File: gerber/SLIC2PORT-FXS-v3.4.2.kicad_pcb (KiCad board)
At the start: 2 copper layers, 120 x 90 mm, 160 parts, among them J1 USB-C_PWR, J2 DC5V_IN, J5 EXPANSION, J6 UART_DBG, K1 G5V-2_DC5, K2 G5V-2_DC5, Q1 AO3401A, Q2 2N7002, Q3 2N7002, Q4 2N7002, Q5 2N7002, Q6 2N7002, SW1 RST, SW2 BOOT, U1 M5StampS3/S3A, U106 1N5819, U2 74HCT244, U45 1N4007, U49 1N4007, U55 P3100SC, U56 1N4007, U57 1N4007, U58 1N4007, U59 1N4007, U60 BZT03C82, U64 BK2125HS601-T, U79 1N5819, U82 P3100SC, U83 1N4007, U84 1N4007, U85 1N4007, U86 1N4007, U87 BZT03C82, U91 BK2125HS601-T

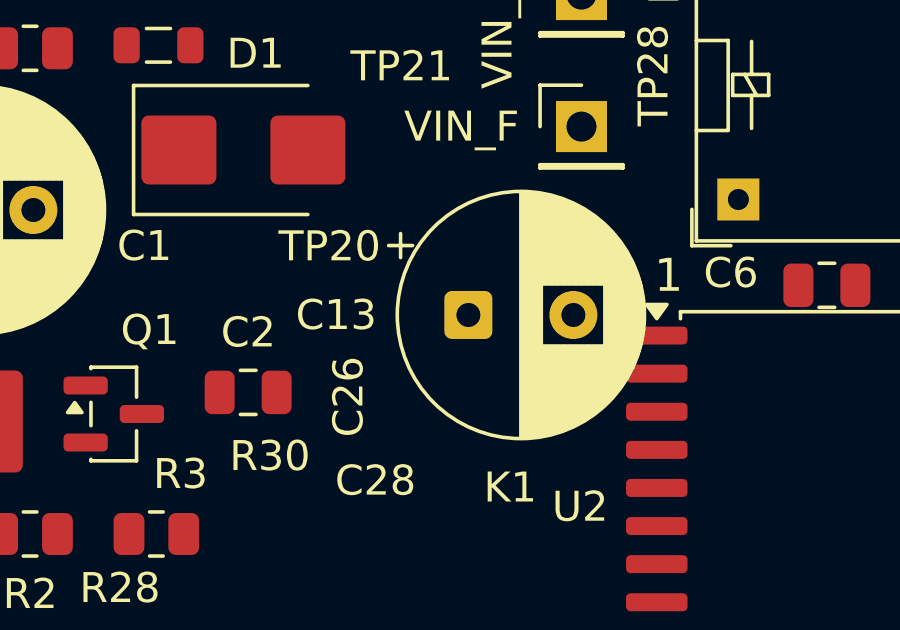
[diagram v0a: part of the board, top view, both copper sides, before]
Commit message: board v3.4.2: 第9ラウンド処方 (C13 -1.0mm) を適用し第10ラウンドとして記録
- C13 を X -1.00mm へ移動 (生成元にも同期、check_regen 0/0 維持)。
  U2 パッド1/2 との干渉 -0.474/-0.124mm -> +0.521/+0.799mm を実測で再現
- RJ11 是正ラウンドは監査側の第9ラウンド (コンデンサ監査) と重なるため
  第10ラウンドとして CAD_REPORT に記録し、生成元の表記も round 10 に整合
- README_CAD の RJ11 項を想定寸法から指定部品の実寸仕様へ更新
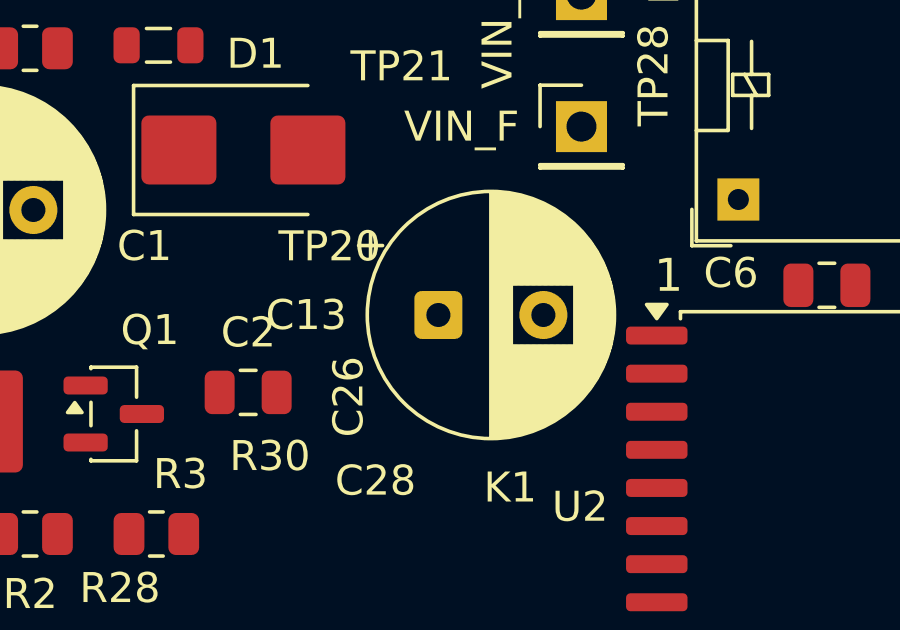
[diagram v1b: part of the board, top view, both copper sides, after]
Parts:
- moved C13 1.00 mm to (21.5, 65.3)
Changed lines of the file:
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@@
 		)
 		(attr through_hole)
+		(duplicate_pad_numbers_are_jumpers no)
 		(fp_line
-			(start -6.10 -6.00)
-			(end 6.10 -6.00)
+			(start -6.1 -6)
+			(end 6.1 -6)
 			(stroke
 				(width 0.12)
@@
 		)
 		(fp_line
-			(start 6.10 -6.00)
-			(end 6.10 9.00)
+			(start -6.1 9)
+			(end -6.1 -6)
 			(stroke
 				(width 0.12)
@@
 		)
 		(fp_line
-			(start 6.10 9.00)
-			(end -6.10 9.00)
+			(start 6.1 -6)
+			(end 6.1 9)
 			(stroke
 				(width 0.12)
@@
 		)
 		(fp_line
-			(start -6.10 9.00)
-			(end -6.10 -6.00)
+			(start 6.1 9)
+			(end -6.1 9)
 			(stroke
 				(width 0.12)
@@
 			(layer "F.SilkS")
 		)
-		(fp_line
-			(start -6.35 -6.30)
-			(end 6.35 -6.30)
+		(fp_circle
+			(center 4.35 4.64)
+			(end 4.85 4.64)
 			(stroke
-				(width 0.05)
+				(width 0.12)
 				(type solid)
 			)
-			(layer "F.CrtYd")
+			(fill no)
+			(layer "F.SilkS")
 		)
 		(fp_line
-			(start 6.35 -6.30)
-			(end 6.35 9.30)
+			(start -6.35 -6.3)
+			(end 6.35 -6.3)
 			(stroke
 				(width 0.05)
@@
 		)
 		(fp_line
-			(start 6.35 9.30)
-			(end -6.35 9.30)
+			(start -6.35 9.3)
+			(end -6.35 -6.3)
 			(stroke
 				(width 0.05)
@@
 		)
 		(fp_line
-			(start -6.35 9.30)
-			(end -6.35 -6.30)
+			(start 6.35 -6.3)
+			(end 6.35 9.3)
 			(stroke
 				(width 0.05)
@@
 			(layer "F.CrtYd")
 		)
-		(fp_circle
-			(center 4.35 4.64)
-			(end 4.85 4.64)
+		(fp_line
+			(start 6.35 9.3)
+			(end -6.35 9.3)
 			(stroke
-				(width 0.12)
+				(width 0.05)
 				(type solid)
 			)
-			(fill no)
-			(layer "F.SilkS")
+			(layer "F.CrtYd")
 		)
-		(duplicate_pad_numbers_are_jumpers no)
 		(pad "" np_thru_hole circle
 			(at -6 0)
@@
 	(footprint "CP_Radial_D8.0mm_P3.50mm"
 		(layer "F.Cu")
-		(at 22.525 65.275)
+		(at 21.525 65.275)
 		(descr "CP, Radial series, Radial, pin pitch=3.50mm, diameter=8mm, height=12mm, Electrolytic Capacitor")
 		(tags "CP Radial series Radial pin pitch 3.50mm diameter 8mm height 12mm Electrolytic Capacitor")
@@
 		)
 		(attr through_hole)
+		(duplicate_pad_numbers_are_jumpers no)
 		(fp_line
-			(start -6.10 -6.00)
-			(end 6.10 -6.00)
+			(start -6.1 -6)
+			(end 6.1 -6)
 			(stroke
 				(width 0.12)
@@
 		)
 		(fp_line
-			(start 6.10 -6.00)
-			(end 6.10 9.00)
+			(start -6.1 9)
+			(end -6.1 -6)
 			(stroke
 				(width 0.12)
@@
 		)
 		(fp_line
-			(start 6.10 9.00)
-			(end -6.10 9.00)
+			(start 6.1 -6)
+			(end 6.1 9)
 			(stroke
 				(width 0.12)
@@
 		)
 		(fp_line
-			(start -6.10 9.00)
-			(end -6.10 -6.00)
+			(start 6.1 9)
+			(end -6.1 9)
 			(stroke
 				(width 0.12)
@@
 			(layer "F.SilkS")
 		)
-		(fp_line
-			(start -6.35 -6.30)
-			(end 6.35 -6.30)
+		(fp_circle
+			(center 4.35 4.64)
+			(end 4.85 4.64)
 			(stroke
-				(width 0.05)
+				(width 0.12)
 				(type solid)
 			)
-			(layer "F.CrtYd")
+			(fill no)
+			(layer "F.SilkS")
 		)
 		(fp_line
-			(start 6.35 -6.30)
-			(end 6.35 9.30)
+			(start -6.35 -6.3)
+			(end 6.35 -6.3)
 			(stroke
 				(width 0.05)
@@
 		)
 		(fp_line
-			(start 6.35 9.30)
-			(end -6.35 9.30)
+			(start -6.35 9.3)
+			(end -6.35 -6.3)
 			(stroke
 				(width 0.05)
@@
 		)
 		(fp_line
-			(start -6.35 9.30)
-			(end -6.35 -6.30)
+			(start 6.35 -6.3)
+			(end 6.35 9.3)
 			(stroke
 				(width 0.05)
@@
 			(layer "F.CrtYd")
 		)
-		(fp_circle
-			(center 4.35 4.64)
-			(end 4.85 4.64)
+		(fp_line
+			(start 6.35 9.3)
+			(end -6.35 9.3)
 			(stroke
-				(width 0.12)
+				(width 0.05)
 				(type solid)
 			)
-			(fill no)
-			(layer "F.SilkS")
+			(layer "F.CrtYd")
 		)
-		(duplicate_pad_numbers_are_jumpers no)
 		(pad "" np_thru_hole circle
 			(at -6 0)
